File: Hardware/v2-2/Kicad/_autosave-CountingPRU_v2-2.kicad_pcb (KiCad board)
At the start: 2 copper layers, 160 x 100 mm, 94 parts, among them J1 BBB, J2 IN_ETHERNET, J3 BERGOZ_02, J4 BERGOZ_01, P1 LNLS, P2 LNLS, Q1 BSR14, Q2 BSR14, Q3 BSR14, T1 Module-XFRMR-POE, T2 CMC, T3 CMC, U1 741G74, U10 1G125, U11 1G125, U12 1G04, U13 1G04, U14 TS5A21366, U15 TS5A21366, U16 Ag9205, U17 VIBLSD1-S5-S5-DIP, U18 MEV1D0512DC, U19 1G08, U2 741G74, U20 TS5A21366, U21 74LS123, U22 1G08, U23 741G74, U24 741G74, U25 1G125, U26 1G125, U3 741G74, U4 741G74, U5 741G74, U6 741G74, U7 1G04, U8 1G125, U9 1G125

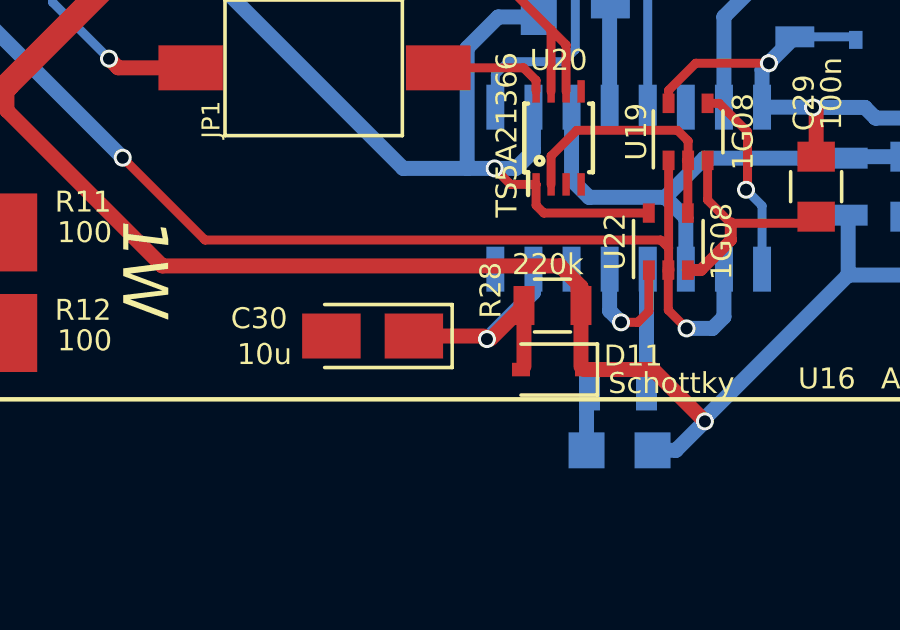
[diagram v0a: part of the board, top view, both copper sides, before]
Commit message: Config pins for kernel 4.14 added
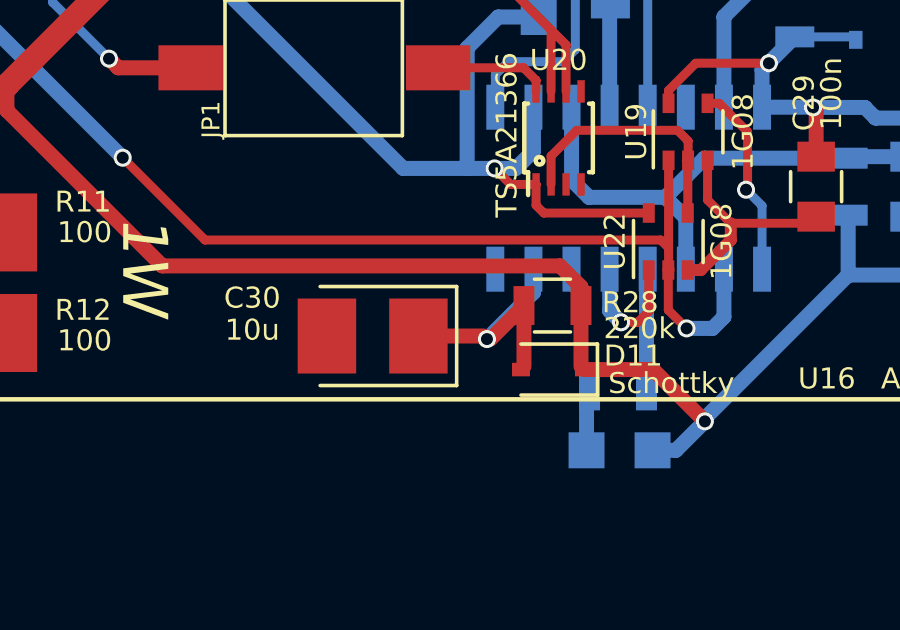
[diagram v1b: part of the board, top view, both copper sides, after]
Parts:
- C30: footprint Capacitors_Tantalum_SMD:CP_Tantalum_Case-A_EIA-3216-18_Reflow -> Capacitors_Tantalum_SMD:CP_Tantalum_Case-T_EIA-3528-12_Reflow
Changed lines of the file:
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@@
   (layers
     (0 F.Cu signal)
-    (31 B.Cu signal)
+    (31 B.Cu signal hide)
     (32 B.Adhes user)
     (33 F.Adhes user)
@@
     (pad_to_mask_clearance 0.2)
     (aux_axis_origin 0 0)
-    (grid_origin 45.54724 67.31)
     (visible_elements FFFFDFFF)
     (pcbplotparams
@@
     (add_net "Net-(U6-Pad3)")
   )
+  (module Capacitors_Tantalum_SMD:CP_Tantalum_Case-T_EIA-3528-12_Reflow (layer F.Cu)
+    (at 122.15364 94.6912 180)
+    (descr "Tantalum capacitor, Case T, EIA 3528-12, 3.5x2.8x1.2mm, Reflow soldering footprint")
+    (tags "capacitor tantalum smd")
+    (attr smd)
+    (fp_text reference C30 (at 4.0132 1.27 180) (layer F.SilkS)
+      (effects (font (size 0.7 0.7) (thickness 0.15)))
+    )
+    (fp_text value 10u (at 4.0132 0.2032 180) (layer F.SilkS)
+      (effects (font (size 0.7 0.7) (thickness 0.15)))
+    )
+    (fp_text user "" (at 0 0 180) (layer F.Fab)
+      (effects (font (size 0.8 0.8) (thickness 0.12)))
+    )
+    (fp_line (start -2.85 -1.75) (end -2.85 1.75) (layer F.CrtYd) (width 0.05))
+    (fp_line (start -2.85 1.75) (end 2.85 1.75) (layer F.CrtYd) (width 0.05))
+    (fp_line (start 2.85 1.75) (end 2.85 -1.75) (layer F.CrtYd) (width 0.05))
+    (fp_line (start 2.85 -1.75) (end -2.85 -1.75) (layer F.CrtYd) (width 0.05))
+    (fp_line (start -1.75 -1.4) (end -1.75 1.4) (layer F.Fab) (width 0.1))
+    (fp_line (start -1.75 1.4) (end 1.75 1.4) (layer F.Fab) (width 0.1))
+    (fp_line (start 1.75 1.4) (end 1.75 -1.4) (layer F.Fab) (width 0.1))
+    (fp_line (start 1.75 -1.4) (end -1.75 -1.4) (layer F.Fab) (width 0.1))
+    (fp_line (start -1.4 -1.4) (end -1.4 1.4) (layer F.Fab) (width 0.1))
+    (fp_line (start -1.225 -1.4) (end -1.225 1.4) (layer F.Fab) (width 0.1))
+    (fp_line (start -2.8 -1.65) (end 1.75 -1.65) (layer F.SilkS) (width 0.12))
+    (fp_line (start -2.8 1.65) (end 1.75 1.65) (layer F.SilkS) (width 0.12))
+    (fp_line (start -2.8 -1.65) (end -2.8 1.65) (layer F.SilkS) (width 0.12))
+    (pad 1 smd rect (at -1.525 0 180) (size 1.95 2.5) (layers F.Cu F.Paste F.Mask)
+      (net 147 "Net-(C30-Pad1)"))
+    (pad 2 smd rect (at 1.525 0 180) (size 1.95 2.5) (layers F.Cu F.Paste F.Mask)
+      (net 1 GND))
+    (model Capacitors_Tantalum_SMD.3dshapes/CP_Tantalum_Case-T_EIA-3528-12.wrl
+      (at (xyz 0 0 0))
+      (scale (xyz 1 1 1))
+      (rotate (xyz 0 0 0))
+    )
+  )
   (module CONTROLE:TSSOP-8 (layer F.Cu)
     (at 86.42524 66 270)
@@
     (tags "resistor 0805")
     (attr smd)
-    (fp_text reference R28 (at 2.0574 0.508 270) (layer F.SilkS)
+    (fp_text reference R28 (at -2.5908 0.1016 180) (layer F.SilkS)
       (effects (font (size 0.7 0.7) (thickness 0.15)))
     )
-    (fp_text value 220k (at 0.1524 1.3716 180) (layer F.SilkS)
+    (fp_text value 220k (at -2.8956 -0.762 180) (layer F.SilkS)
       (effects (font (size 0.7 0.7) (thickness 0.15)))
     )
@@
       (at (xyz 0 0 0))
       (scale (xyz 1 1 1))
-      (rotate (xyz 0 0 0))
-    )
-  )
-  (module Capacitors_Tantalum_SMD:CP_Tantalum_Case-A_EIA-3216-18_Reflow (layer F.Cu)
-    (at 122.15364 94.6912 180)
-    (descr "Tantalum capacitor, Case A, EIA 3216-18, 3.2x1.6x1.6mm, Reflow soldering footprint")
-    (tags "capacitor tantalum smd")
-    (attr smd)
-    (fp_text reference C30 (at 3.7846 0.5842 180) (layer F.SilkS)
-      (effects (font (size 0.7 0.7) (thickness 0.15)))
-    )
-    (fp_text value 10u (at 3.6068 -0.6096 180) (layer F.SilkS)
-      (effects (font (size 0.7 0.7) (thickness 0.15)))
-    )
-    (fp_text user %R (at 0 0 180) (layer F.Fab)
-      (effects (font (size 0.7 0.7) (thickness 0.105)))
-    )
-    (fp_line (start -2.75 -1.2) (end -2.75 1.2) (layer F.CrtYd) (width 0.05))
-    (fp_line (start -2.75 1.2) (end 2.75 1.2) (layer F.CrtYd) (width 0.05))
-    (fp_line (start 2.75 1.2) (end 2.75 -1.2) (layer F.CrtYd) (width 0.05))
-    (fp_line (start 2.75 -1.2) (end -2.75 -1.2) (layer F.CrtYd) (width 0.05))
-    (fp_line (start -1.6 -0.8) (end -1.6 0.8) (layer F.Fab) (width 0.1))
-    (fp_line (start -1.6 0.8) (end 1.6 0.8) (layer F.Fab) (width 0.1))
-    (fp_line (start 1.6 0.8) (end 1.6 -0.8) (layer F.Fab) (width 0.1))
-    (fp_line (start 1.6 -0.8) (end -1.6 -0.8) (layer F.Fab) (width 0.1))
-    (fp_line (start -1.28 -0.8) (end -1.28 0.8) (layer F.Fab) (width 0.1))
-    (fp_line (start -1.12 -0.8) (end -1.12 0.8) (layer F.Fab) (width 0.1))
-    (fp_line (start -2.65 -1.05) (end 1.6 -1.05) (layer F.SilkS) (width 0.12))
-    (fp_line (start -2.65 1.05) (end 1.6 1.05) (layer F.SilkS) (width 0.12))
-    (fp_line (start -2.65 -1.05) (end -2.65 1.05) (layer F.SilkS) (width 0.12))
-    (pad 1 smd rect (at -1.375 0 180) (size 1.95 1.5) (layers F.Cu F.Paste F.Mask)
-      (net 147 "Net-(C30-Pad1)"))
-    (pad 2 smd rect (at 1.375 0 180) (size 1.95 1.5) (layers F.Cu F.Paste F.Mask)
-      (net 1 GND))
-    (model Capacitors_Tantalum_SMD.3dshapes/CP_Tantalum_Case-A_EIA-3216-18.wrl
-      (at (xyz 0 0 0))
-      (scale (xyz 1 1 1))
